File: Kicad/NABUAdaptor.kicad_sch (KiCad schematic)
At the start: 102 parts, among them J1 Conn_01x04, J2 DIN-5_180degree, J3 Conn_01x09, J4 Conn_01x05, U1 74LS164, U10 UA9638CD, U11 UA9637, U12 74LS164, U13 74LS164, U14 74LS04, U15 74LS74, U16 N8X60, U17 2114, U18 2114, U19 LM339, U2 74LS30, U20 74LS164, U21 74LS86, U22 74LS74, U23 74LS00, U24 74LS04, U25 74LS00, U26 74LS74, U27 74LS00, U28 74LS74, U29 74LS74, U3 74LS27, U30 74LS02, U31 MC6805P2, U32 74LS74, U33 74HCU04, U4 74LS164, U5 PAL16R6 (ID PAL), U6 74LS374, U7 74LS373, U8 ?VALUE?, U9 TR1865PL, Y1 3.579545MHz

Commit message: resize for A1, tweak layout
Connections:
- net MCU_NUM: no longer names the net of JP1.2, R15.2, U31.6 (NUM)
- net UART_DRR_RRD renamed UART_~{DRR}_RRD
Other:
- note added: "MICROCONTROLLER"
- moved on the sheet: C2, C21, C24, C37, C38, C4, C40, C8, CR1, CR2, CR3, CRxxx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

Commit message: huge cleanup, rename some nets based on function
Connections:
- net FIFO_WRITE_QUAL: now reaches U15.2 (D), U22.9 (Q), U27.10
- net DEMOD_DATA_DLY1BIT: now reaches TP1.1, U1.3 (Q0), U14.1, U4.1 (DSA)
- net DEMOD_CLK_DESTUFFED: now reaches TP2.1, U22.3 (C), U24.13, U3.12, U4.8 (CP)
- net CABLEDCK renamed CABLE_BYTECLK
- net CABLEDCK_PRE: no longer names the net of U14.9, U15.9 (Q), U29.11 (C)
- net FIFO_WRITE: no longer names the net of U23.11, U27.9
- net PAL_P13 renamed PAL_P13_MCU_PC2
- net PAL_P14 renamed PAL_P14_MCU_PC3
- net PAL_P19 renamed HDLC_FLAG_Q
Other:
- note added: "Destuffed Bit Clock (Clock suppressed if a zero-stuffing bit is currently on DEMOD_DATA_DLY1BIT)"
- note added: "FLAG/STUFFING DETECTION SHIFT REGISTER"
- note added: "HDLC flag detect, qualified"
- note added: "Incoming bit clock, suppressed for stuffed zeroes"
- note added: "Incoming data with 1-bit delay"
- note added: "PAL P12: Set when MCU PB0=1. Cleared when ~{MCU_INT} active"
- note added: "RECEIVE SHIFT REGISTER"
- note added: "SDLC FLAG DETECTION AND DESTUFFING"
- note added: "U1.Q[7..0] = 0111_1110 (HDLC Flag?)"
- note added: "U1.Q[7..0] = x011_1110 (HDLC stuffed byte?)"
- note removed: "BIT SHIFTER"
- note removed: "BYTE RX SHIFTER"
- note removed: "SYNC DETECTOR?"
- note removed: "U1.Q[7..0] = 0011_1110"
- note removed: "U1.Q[7..0] = 0111_1110"
- moved on the sheet: R10, R12, R13, R14, R4, R9, TP1, TP2, TP4, TP5, U14D, U15A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

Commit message: fix up PLL/demod pin names
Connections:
- net PLL_P2 renamed PLL_P2_ENB
- net PLL_P3 renamed PLL_P3_RSSI
- net PLL_P4 renamed PLL_P4_CLOCK
- net PLL_P5 renamed PLL_P5_DATA
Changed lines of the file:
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@@
     )
   )
-  (global_label "PLL_P2" (shape input) (at 476.885 415.925 0) (fields_autoplaced)
-    (effects (font (size 1.27 1.27)) (justify left))
-    (property "Intersheetrefs" "${INTERSHEET_REFS}" (at 486.6435 415.925 0)
-      (effects (font (size 1.27 1.27)) (justify left))
-    )
-  )
-  (global_label "PLL_P3" (shape input) (at 598.17 416.56 180) (fields_autoplaced)
-    (effects (font (size 1.27 1.27)) (justify right))
-    (property "Intersheetrefs" "${INTERSHEET_REFS}" (at 588.4115 416.56 0)
+  (global_label "PLL_P2_ENB" (shape output) (at 476.885 415.925 0) (fields_autoplaced)
+    (effects (font (size 1.27 1.27)) (justify left))
+    (property "Intersheetrefs" "${INTERSHEET_REFS}" (at 491.3606 415.925 0)
+      (effects (font (size 1.27 1.27)) (justify left))
+    )
+  )
+  (global_label "PLL_P3_RSSI" (shape input) (at 598.17 416.56 180) (fields_autoplaced)
+    (effects (font (size 1.27 1.27)) (justify right))
+    (property "Intersheetrefs" "${INTERSHEET_REFS}" (at 583.1501 416.56 0)
       (effects (font (size 1.27 1.27)) (justify right))
     )
@@
     )
   )
-  (global_label "PLL_P5" (shape input) (at 630.555 63.5 0) (fields_autoplaced)
-    (effects (font (size 1.27 1.27)) (justify left))
-    (property "Intersheetrefs" "${INTERSHEET_REFS}" (at 640.3135 63.5 0)
-      (effects (font (size 1.27 1.27)) (justify left))
-    )
-  )
-  (global_label "PLL_P5" (shape input) (at 782.32 121.285 0) (fields_autoplaced)
-    (effects (font (size 1.27 1.27)) (justify left))
-    (property "Intersheetrefs" "${INTERSHEET_REFS}" (at 792.0785 121.285 0)
+  (global_label "PLL_P5_DATA" (shape input) (at 630.555 63.5 0) (fields_autoplaced)
+    (effects (font (size 1.27 1.27)) (justify left))
+    (property "Intersheetrefs" "${INTERSHEET_REFS}" (at 645.6959 63.5 0)
+      (effects (font (size 1.27 1.27)) (justify left))
+    )
+  )
+  (global_label "PLL_P5_DATA" (shape input) (at 782.32 121.285 0) (fields_autoplaced)
+    (effects (font (size 1.27 1.27)) (justify left))
+    (property "Intersheetrefs" "${INTERSHEET_REFS}" (at 797.4609 121.285 0)
       (effects (font (size 1.27 1.27)) (justify left))
     )
@@
     )
   )
-  (global_label "PLL_P4" (shape input) (at 782.32 118.745 0) (fields_autoplaced)
-    (effects (font (size 1.27 1.27)) (justify left))
-    (property "Intersheetrefs" "${INTERSHEET_REFS}" (at 792.0785 118.745 0)
+  (global_label "PLL_P4_CLOCK" (shape input) (at 782.32 118.745 0) (fields_autoplaced)
+    (effects (font (size 1.27 1.27)) (justify left))
+    (property "Intersheetrefs" "${INTERSHEET_REFS}" (at 799.2147 118.745 0)
       (effects (font (size 1.27 1.27)) (justify left))
     )
@@
     )
   )
-  (global_label "PLL_P3" (shape input) (at 782.32 116.205 0) (fields_autoplaced)
-    (effects (font (size 1.27 1.27)) (justify left))
-    (property "Intersheetrefs" "${INTERSHEET_REFS}" (at 792.0785 116.205 0)
+  (global_label "PLL_P3_RSSI" (shape output) (at 782.32 116.205 0) (fields_autoplaced)
+    (effects (font (size 1.27 1.27)) (justify left))
+    (property "Intersheetrefs" "${INTERSHEET_REFS}" (at 797.3399 116.205 0)
       (effects (font (size 1.27 1.27)) (justify left))
     )
@@
     )
   )
-  (global_label "PLL_P2" (shape input) (at 782.32 113.665 0) (fields_autoplaced)
-    (effects (font (size 1.27 1.27)) (justify left))
-    (property "Intersheetrefs" "${INTERSHEET_REFS}" (at 792.0785 113.665 0)
+  (global_label "PLL_P2_ENB" (shape input) (at 782.32 113.665 0) (fields_autoplaced)
+    (effects (font (size 1.27 1.27)) (justify left))
+    (property "Intersheetrefs" "${INTERSHEET_REFS}" (at 796.7956 113.665 0)
       (effects (font (size 1.27 1.27)) (justify left))
     )
@@
     )
   )
-  (global_label "PLL_P4" (shape output) (at 630.555 103.505 0) (fields_autoplaced)
-    (effects (font (size 1.27 1.27)) (justify left))
-    (property "Intersheetrefs" "${INTERSHEET_REFS}" (at 640.3135 103.505 0)
-      (effects (font (size 1.27 1.27)) (justify left))
-    )
+  (global_label "PLL_P4_CLOCK" (shape output) (at 630.555 103.505 0) (fields_autoplaced)
+    (effects (font (size 1.27 1.27)) (justify left))
+    (property "Intersheetrefs" "${INTERSHEET_REFS}" (at 647.4497 103.505 0)
+      (effects (font (size 1.27 1.27)) (justify left))
+    )

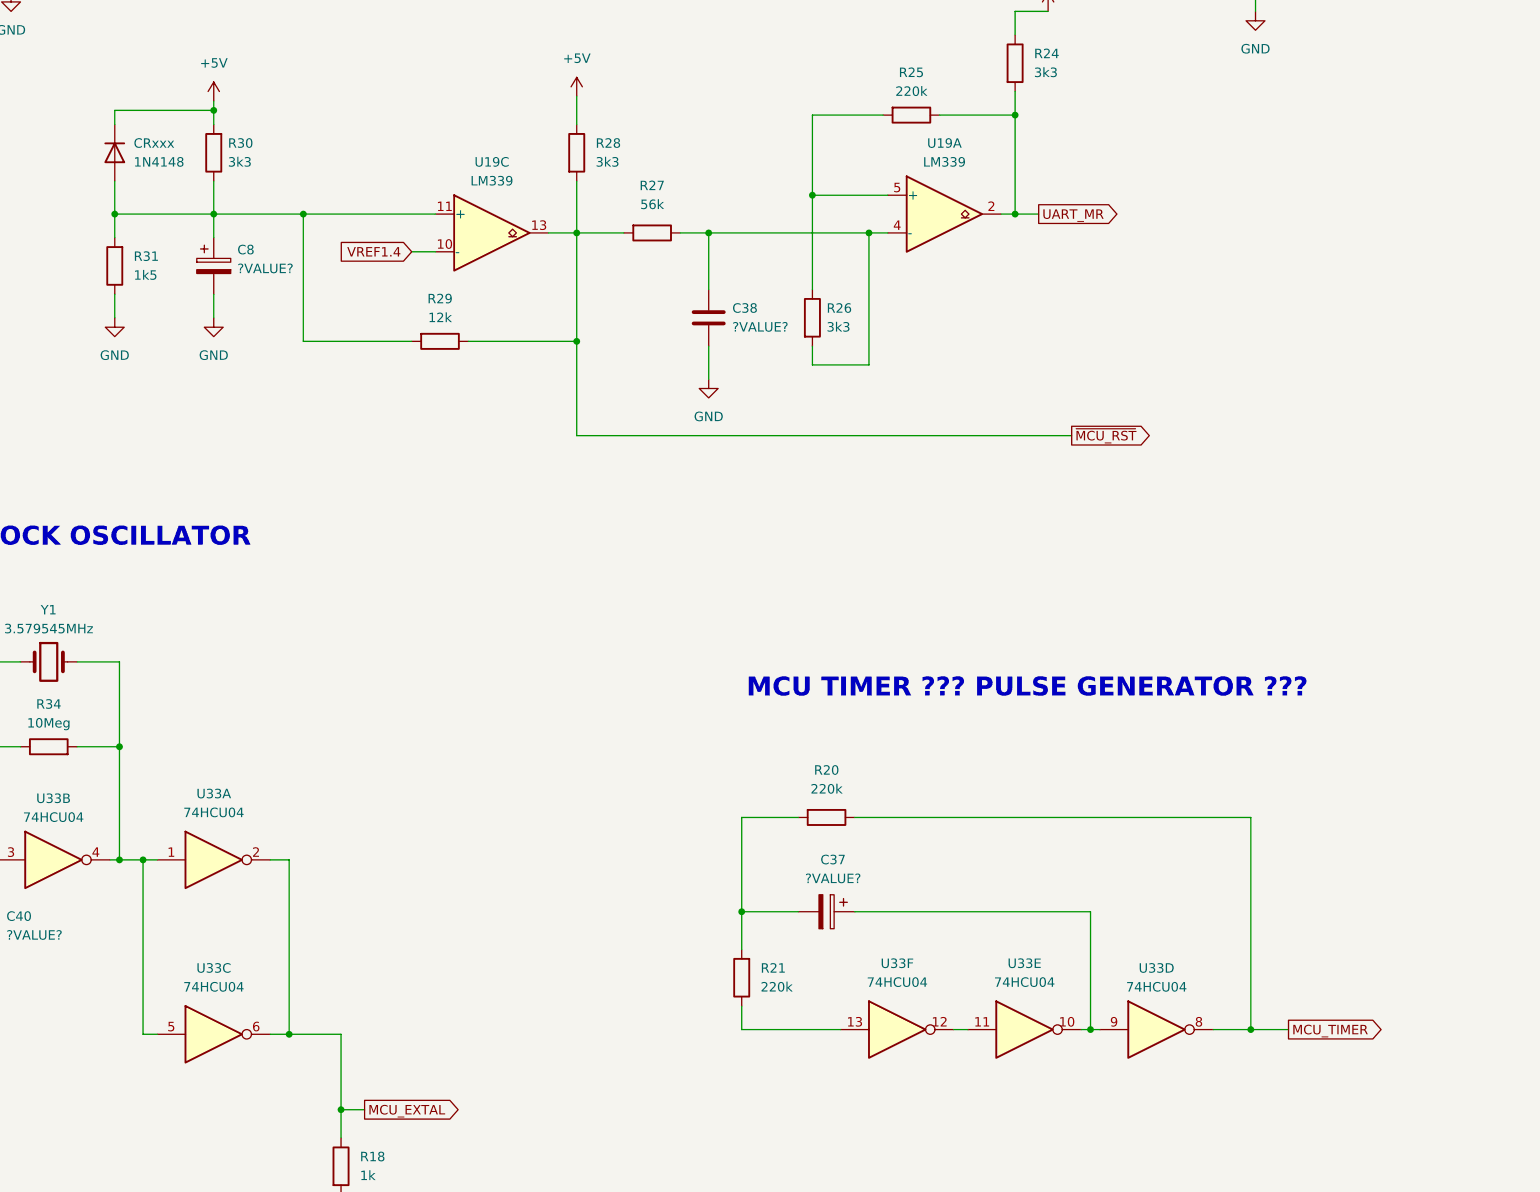
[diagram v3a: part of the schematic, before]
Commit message: clean up MCU timer osc, add C37 value, calculate frequency
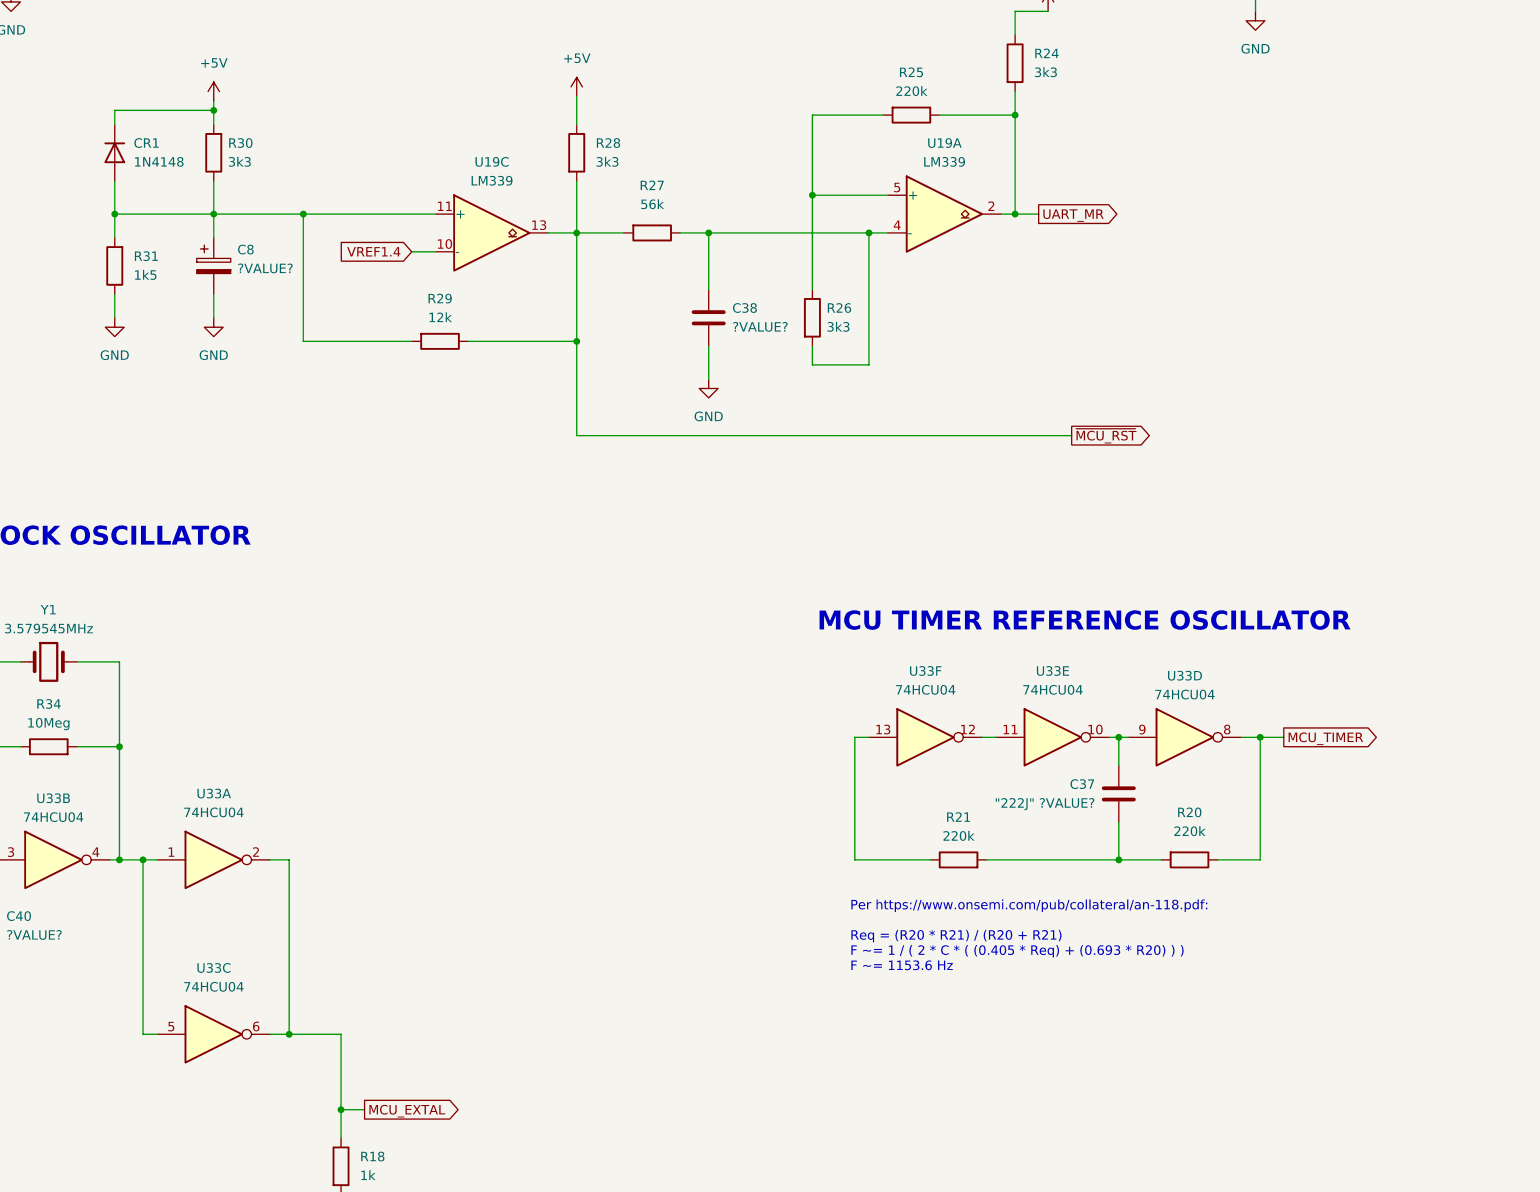
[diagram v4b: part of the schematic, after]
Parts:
- removed C37: ?VALUE?, symbol Device:C_Polarized
- added C37: "222J" ?VALUE?, symbol Device:C
- renumbered CRxxx to CR1
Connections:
- net at U33.10, U33.9: now also C37.2
- net at R20.2, R21.2: now also C37.1
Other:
- note added: "MCU TIMER REFERENCE OSCILLATOR"
- note added: "Per https://www.onsemi.com/pub/collateral/an-118.pdf: Req = (R20 * R21) / (R20 + R21) F ~= 1 / ( 2 * C * ( (0.405 * Req) + (0.693 * R20) ) ) F ~= 1153.6 Hz"
- note removed: "MCU TIMER ??? PULSE GENERATOR ???"
- moved on the sheet: R20, R21, U33D, U33E, U33F
